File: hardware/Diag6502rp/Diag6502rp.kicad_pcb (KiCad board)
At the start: 4 copper layers, 59.5 x 54.3 mm, 83 parts, among them J1 Conn_01x20_PinHeader, J10 Conn_01x20_PinHeader, J11 Conn_01x20_PinHeader, J2 Conn_01x20_PinSocket, J3 Conn_01x20_PinHeader, J4 Conn_01x20_PinSocket, J5 GT-USB-7010AN, J6 Conn_02x20_Counter_Clockwise, J7 Conn_ARM_SWD_TagConnect_TC2030, J8 Conn_01x02_PinSocket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

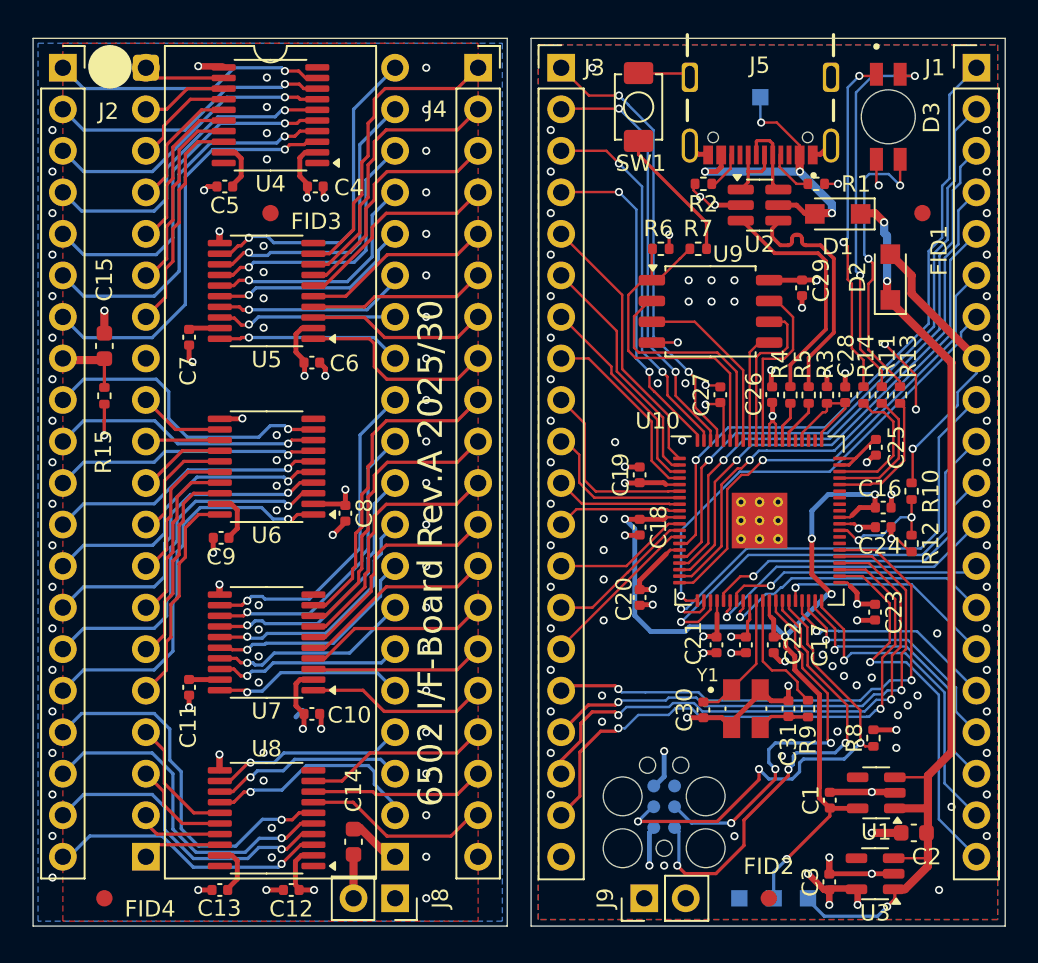
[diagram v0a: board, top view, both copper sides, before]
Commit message: More via separation and transfer vias
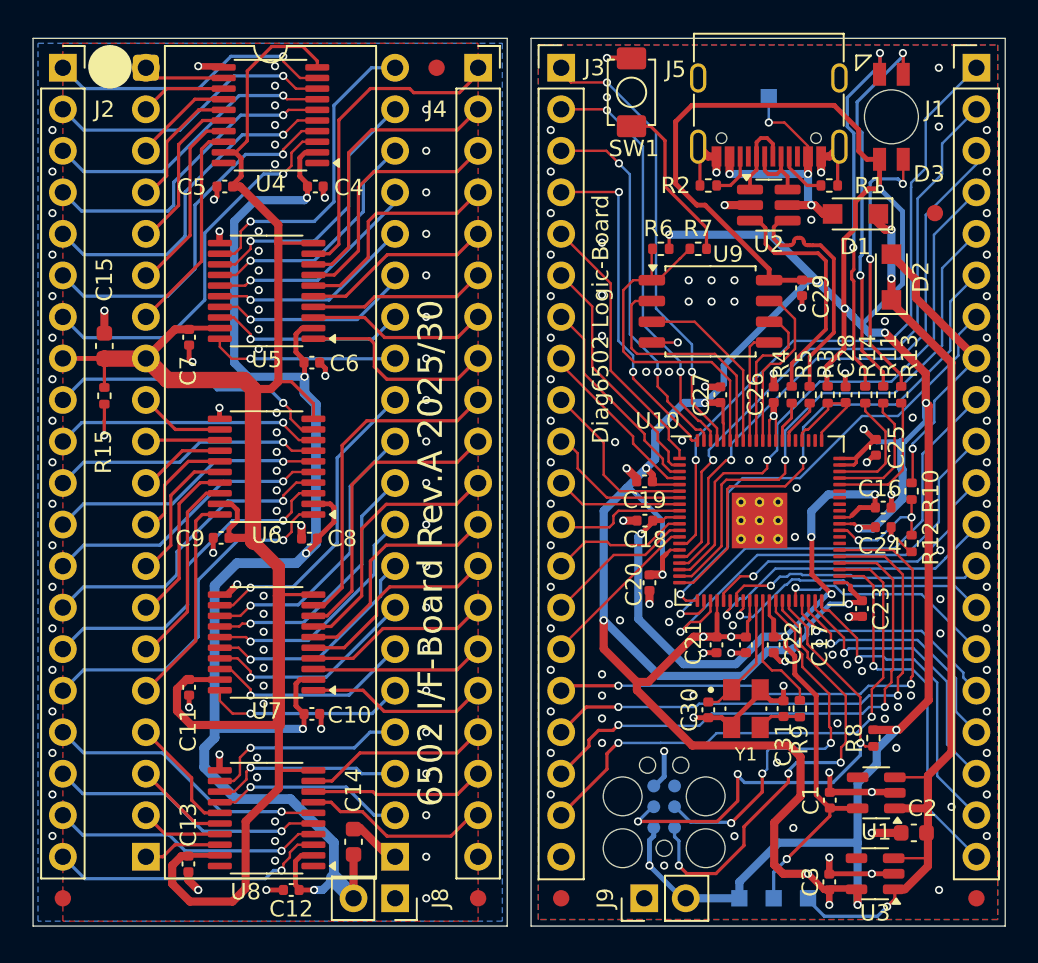
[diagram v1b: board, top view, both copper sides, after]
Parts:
- added FID5: Fiducial_1mm_Mask2mm, Fiducial:Fiducial_1mm_Mask2mm, F.Cu at (127.0, 88.9)
- added FID6: Fiducial_1mm_Mask2mm, Fiducial:Fiducial_1mm_Mask2mm, F.Cu at (152.4, 88.9)
- FID1, FID2, FID3, FID4: value Fiducial -> Fiducial_1mm_Mask2mm
- J5: value GT-USB-7010AN -> GT-USB-7010ASV; footprint footprints:GCT_USB4105-GF-A -> Connector_USB:USB_C_Receptacle_G-Switch_GT-USB-7010ASV
- moved FID4 65.9 mm to (149.9, 47.0)
- moved FID3 43.8 mm to (121.9, 88.9)
- moved FID2 43.2 mm to (96.5, 88.9)
- moved FID1 31.0 mm to (119.4, 38.1)
- moved B2 10.6 mm to (139.4, 36.2)
- moved C8 2.69 mm to (111.6, 66.9), turned to 180 degrees
- moved C13 2.50 mm to (104.2, 86.8), turned to -90 degrees
- moved J5 1.23 mm to (139.7, 39.8)
- moved D1 1.08 mm to (145.0, 47.0)
- moved C20 1.08 mm to (132.4, 69.6)
- moved SW1 1.00 mm to (131.3, 39.6)
- moved C23 0.83 mm to (145.4, 71.2)
- moved R1 0.81 mm to (143.4, 45.3)
- moved U2 0.57 mm to (139.7, 46.5)
- moved TP2 0.52 mm to (139.7, 39.9)
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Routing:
- net +3V3: track 50.1 -> 262.8 mm
- net /Level Shifters & CPU Interface/+5V_I: track 16.9 -> 116.2 mm
- net /Level Shifters & CPU Interface/+3V3_I: track 21.6 -> 91.3 mm
- net /Level Shifters & CPU Interface/CPU_17: track 23.2 -> 17.3 mm
- net /Level Shifters & CPU Interface/CPU_18: track 21.1 -> 17.0 mm
- net GND: track 47.6 -> 51.5 mm, vias 88 -> 109
- net VBUS: track 20.8 -> 17.1 mm
- net /Level Shifters & CPU Interface/CPU_16: track 24.5 -> 22.2 mm
- net /Level Shifters & CPU Interface/CPU_19: track 19.0 -> 16.7 mm
- net /Processor/LED_R: track 20.9 -> 23.1 mm
- net /Processor/A12: track 35.5 -> 33.6 mm
- net /Level Shifters & CPU Interface/PIN_37: track 14.6 -> 12.8 mm
- net /Processor/~{NMI}: track 29.6 -> 31.3 mm
- net /Processor/PIN5: track 31.7 -> 33.3 mm
- net /Level Shifters & CPU Interface/PIN_39: track 18.3 -> 16.8 mm
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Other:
- board text added: "12"
- board text added: "Diag6502"
- board text added: "Diag6502 Logic-Board"
- board text added: "Diag6502 MOS6502 I/F Rev.A TH/2025-07 start-a-dozen.com/diag6502"
- board text added: "Firmware"
- board text added: "Rev.A TH/2025-07"
- board text added: "https://start-a-dozen.com/diag6502"
- board text removed: "A12"
- board text removed: "DIAG6502"
- board text removed: "Diag6502 MOS6502 I/F Rev.A 2025/30 start-a-dozen.com/diag6502"
- board text removed: "Rev.A 2025/30"
- board text removed: "start-a-dozen.com/diag6502"

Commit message: Rev.A
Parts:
- removed J6: Conn_02x20_Counter_Clockwise, Package_DIP:DIP-40_W15.24mm
- moved J10 48.3 mm to (116.8, 38.1), turned to 180 degrees
- moved J11 48.3 mm to (101.6, 38.1), turned to 180 degrees
- moved B2 14.2 mm to (125.2, 36.3)
- moved B1 0.80 mm to (94.7, 36.3)
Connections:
- J10 pad 1: /Level Shifters & CPU Interface/GND_I -> /Level Shifters & CPU Interface/PIN_40
- J10 pad 10: /Level Shifters & CPU Interface/PIN_30 -> /Level Shifters & CPU Interface/PIN_31
- J10 pad 11: /Level Shifters & CPU Interface/PIN_31 -> /Level Shifters & CPU Interface/PIN_30
- J10 pad 12: /Level Shifters & CPU Interface/PIN_32 -> /Level Shifters & CPU Interface/PIN_29
- J10 pad 13: /Level Shifters & CPU Interface/PIN_33 -> /Level Shifters & CPU Interface/PIN_28
- J10 pad 14: /Level Shifters & CPU Interface/PIN_34 -> /Level Shifters & CPU Interface/PIN_27
- J10 pad 15: /Level Shifters & CPU Interface/PIN_35 -> /Level Shifters & CPU Interface/PIN_26
- J10 pad 16: /Level Shifters & CPU Interface/PIN_36 -> /Level Shifters & CPU Interface/PIN_25
- J10 pad 17: /Level Shifters & CPU Interface/PIN_37 -> /Level Shifters & CPU Interface/PIN_24
- J10 pad 18: /Level Shifters & CPU Interface/PIN_38 -> /Level Shifters & CPU Interface/PIN_23
- J10 pad 19: /Level Shifters & CPU Interface/PIN_39 -> /Level Shifters & CPU Interface/PIN_22
- J10 pad 2: /Level Shifters & CPU Interface/PIN_22 -> /Level Shifters & CPU Interface/PIN_39
- J10 pad 20: /Level Shifters & CPU Interface/PIN_40 -> /Level Shifters & CPU Interface/GND_I
- J10 pad 3: /Level Shifters & CPU Interface/PIN_23 -> /Level Shifters & CPU Interface/PIN_38
- J10 pad 4: /Level Shifters & CPU Interface/PIN_24 -> /Level Shifters & CPU Interface/PIN_37
- J10 pad 5: /Level Shifters & CPU Interface/PIN_25 -> /Level Shifters & CPU Interface/PIN_36
- J10 pad 6: /Level Shifters & CPU Interface/PIN_26 -> /Level Shifters & CPU Interface/PIN_35
- J10 pad 7: /Level Shifters & CPU Interface/PIN_27 -> /Level Shifters & CPU Interface/PIN_34
- J10 pad 8: /Level Shifters & CPU Interface/PIN_28 -> /Level Shifters & CPU Interface/PIN_33
- J10 pad 9: /Level Shifters & CPU Interface/PIN_29 -> /Level Shifters & CPU Interface/PIN_32
- J11 pad 1: /Level Shifters & CPU Interface/PIN_20 -> /Level Shifters & CPU Interface/PIN_1
- J11 pad 10: /Level Shifters & CPU Interface/PIN_11 -> /Level Shifters & CPU Interface/PIN_10
- J11 pad 11: /Level Shifters & CPU Interface/PIN_10 -> /Level Shifters & CPU Interface/PIN_11
- J11 pad 12: /Level Shifters & CPU Interface/PIN_9 -> /Level Shifters & CPU Interface/PIN_12
- J11 pad 13: /Level Shifters & CPU Interface/+5V_I -> /Level Shifters & CPU Interface/PIN_13
- J11 pad 14: /Level Shifters & CPU Interface/PIN_7 -> /Level Shifters & CPU Interface/PIN_14
- J11 pad 15: /Level Shifters & CPU Interface/PIN_6 -> /Level Shifters & CPU Interface/PIN_15
- J11 pad 16: /Level Shifters & CPU Interface/PIN_5 -> /Level Shifters & CPU Interface/PIN_16
- J11 pad 17: /Level Shifters & CPU Interface/PIN_4 -> /Level Shifters & CPU Interface/PIN_17
- J11 pad 18: /Level Shifters & CPU Interface/PIN_3 -> /Level Shifters & CPU Interface/PIN_18
- J11 pad 19: /Level Shifters & CPU Interface/PIN_2 -> /Level Shifters & CPU Interface/PIN_19
- J11 pad 2: /Level Shifters & CPU Interface/PIN_19 -> /Level Shifters & CPU Interface/PIN_2
- J11 pad 20: /Level Shifters & CPU Interface/PIN_1 -> /Level Shifters & CPU Interface/PIN_20
- J11 pad 3: /Level Shifters & CPU Interface/PIN_18 -> /Level Shifters & CPU Interface/PIN_3
- J11 pad 4: /Level Shifters & CPU Interface/PIN_17 -> /Level Shifters & CPU Interface/PIN_4
- J11 pad 5: /Level Shifters & CPU Interface/PIN_16 -> /Level Shifters & CPU Interface/PIN_5
- J11 pad 6: /Level Shifters & CPU Interface/PIN_15 -> /Level Shifters & CPU Interface/PIN_6
- J11 pad 7: /Level Shifters & CPU Interface/PIN_14 -> /Level Shifters & CPU Interface/PIN_7
- J11 pad 8: /Level Shifters & CPU Interface/PIN_13 -> /Level Shifters & CPU Interface/+5V_I
- J11 pad 9: /Level Shifters & CPU Interface/PIN_12 -> /Level Shifters & CPU Interface/PIN_9
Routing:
- net +3V3: track 262.8 -> 294.0 mm
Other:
- board text removed: "USB BOOT"
